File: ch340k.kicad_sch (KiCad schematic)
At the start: 8 parts, among them J1 USB_B_Mini, J2 Conn_01x06_Male, U1 CH340K

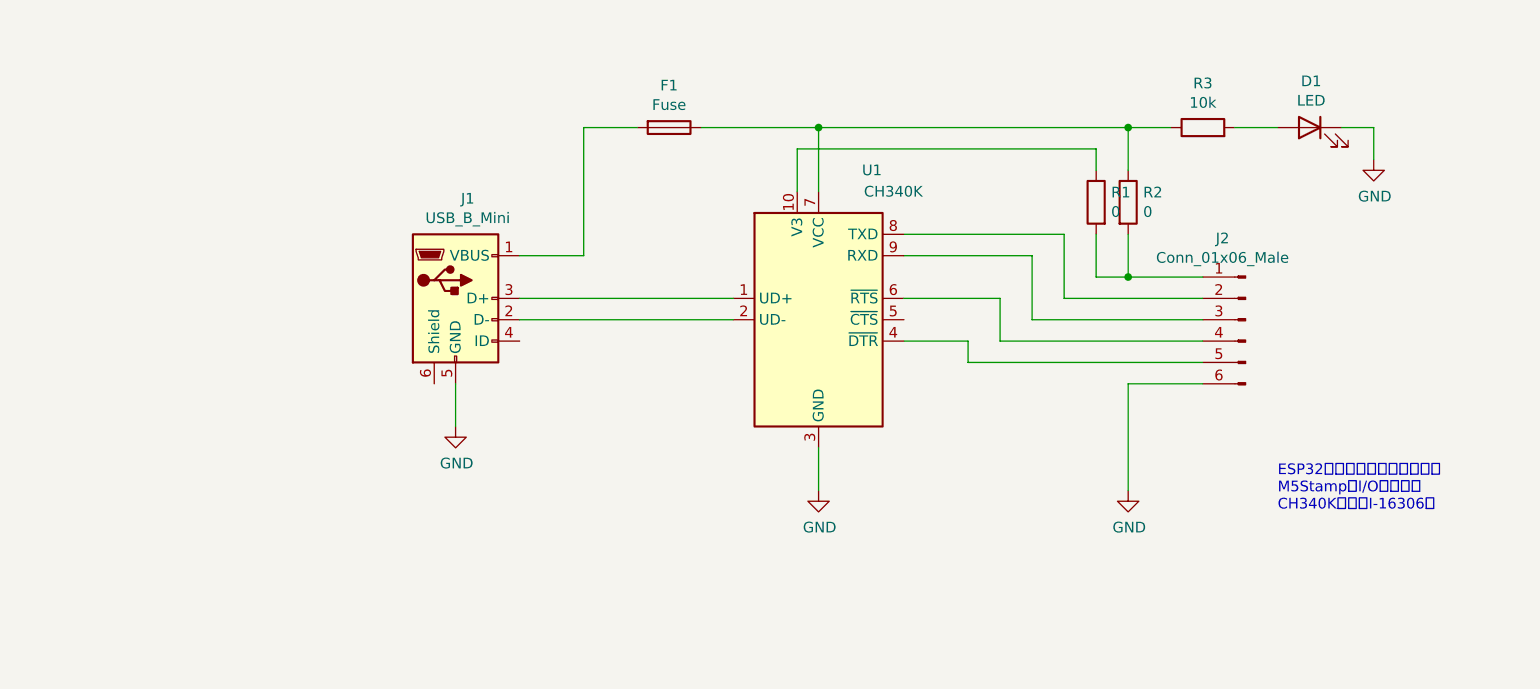
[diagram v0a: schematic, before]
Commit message: M5Stamp/ESP32 Downloader prototype
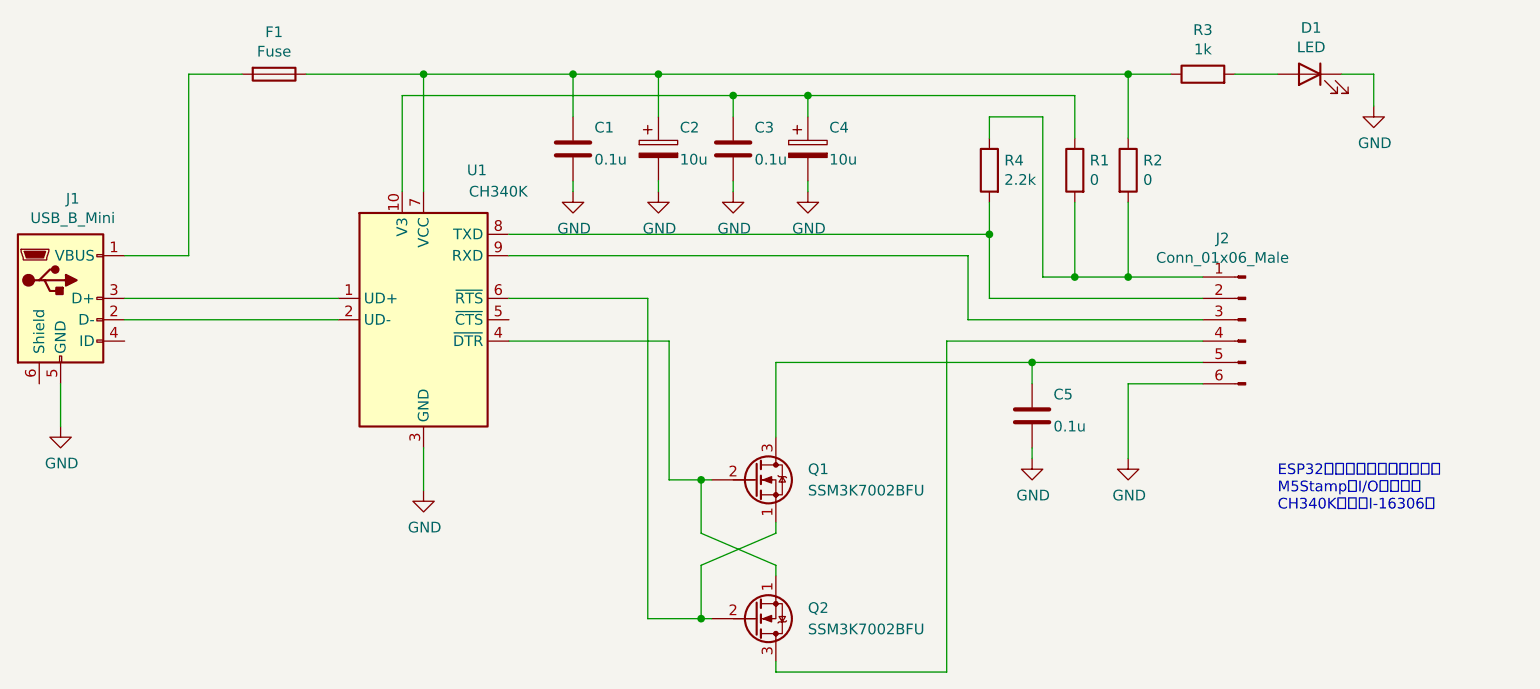
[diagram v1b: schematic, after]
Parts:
- added C1, C3, C5: 0.1u, UserLib:0603, symbol Device:C
- added C2, C4: 10u, Capacitor_THT:CP_Radial_D5.0mm_P2.00mm, symbol Device:C_Polarized
- added Q1, Q2: SSM3K7002BFU, Package_TO_SOT_SMD:SOT-323_SC-70, symbol Device:Q_NMOS_SGD
- added R4: 2.2k, UserLib:0603, symbol Device:R
- D1: footprint digikey-footprints:LED_2-SMD_No_Lead_1.7x0.8mm -> UserLib:0603
- F1, R1, R2: footprint digikey-footprints:0603 -> UserLib:0603
- R3: value 10k -> 1k; footprint digikey-footprints:0603 -> UserLib:0603
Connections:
- net GND: now also C1.2, C2.2, C3.2, C4.2, C5.2
- net at J2.1 (Pin_1), R1.2, R2.2: now also R4.1
- net at J2.2 (Pin_2), U1.8 (TXD): now also R4.2
- net at J2.4 (Pin_4): now also Q2.3 (D); no longer U1.6 (~{RTS})
- net at J2.5 (Pin_5): now also C5.1, Q1.3 (D); no longer U1.4 (~{DTR})
- net at R1.1, U1.10 (V3): now also C3.1, C4.1
- net at F1.1, R2.1, R3.1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: now also C1.1, C2.1
- new net: Q1.2 (G), Q2.1 (S), U1.4 (~{DTR})
- new net: Q1.1 (S), Q2.2 (G), U1.6 (~{RTS})
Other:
- moved on the sheet: D1, F1, J1, R1, R2, R3, U1

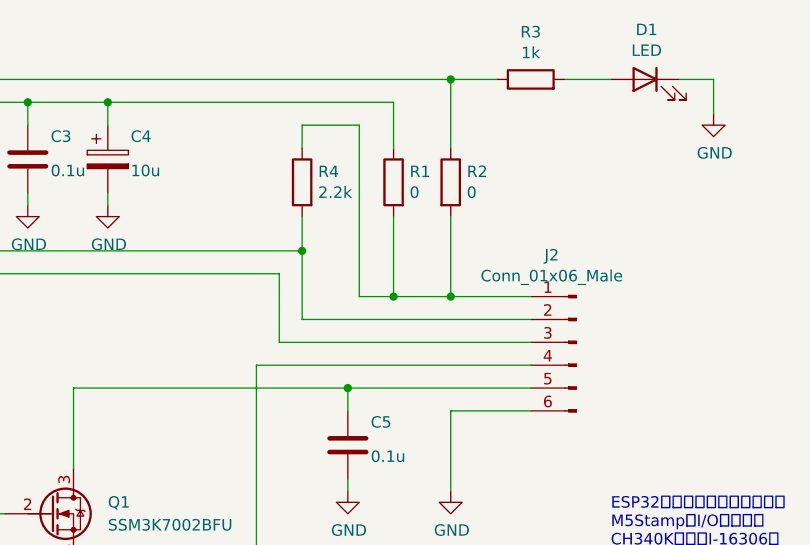
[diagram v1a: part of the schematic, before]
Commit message: Add files via upload
秋月の通販コード追加
部品表の代わりにxmlファイル
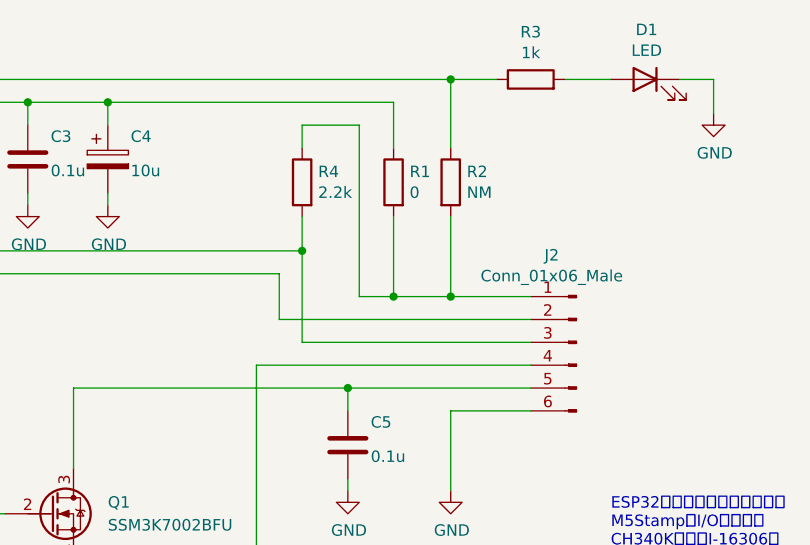
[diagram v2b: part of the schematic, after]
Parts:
- R2: value 0 -> NM
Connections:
- net at R4.2, U1.8 (TXD): now also J2.3 (Pin_3); no longer J2.2 (Pin_2)
- net at U1.9 (RXD): now also J2.2 (Pin_2); no longer J2.3 (Pin_3)
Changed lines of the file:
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@@
   (title_block
     (title "M5Stamp Downloader")
-    (date "2022-03-12")
+    (date "2022-05-03")
     (rev "0")
     (company "JK1MLY")
@@
     (stroke (width 0) (type default) (color 0 0 0 0))
   )
-  (wire (pts (xy 186.69 92.71) (xy 158.75 92.71))
+  (wire (pts (xy 186.69 92.71) (xy 161.29 92.71))
     (stroke (width 0) (type default) (color 0 0 0 0))
   )
@@
     (stroke (width 0) (type default) (color 0 0 0 0))
   )
-  (wire (pts (xy 186.69 90.17) (xy 161.29 90.17))
-    (stroke (width 0) (type default) (color 0 0 0 0))
-  )
   (wire (pts (xy 161.29 71.12) (xy 161.29 68.58))
     (stroke (width 0) (type default) (color 0 0 0 0))
@@
     (stroke (width 0) (type default) (color 0 0 0 0))
   )
+  (wire (pts (xy 186.69 90.17) (xy 158.75 90.17))
+    (stroke (width 0) (type default) (color 0 0 0 0))
+  )
   (wire (pts (xy 58.42 85.09) (xy 66.04 85.09))
     (stroke (width 0) (type default) (color 0 0 0 0))
@@
     (stroke (width 0) (type default) (color 0 0 0 0))
   )
-  (wire (pts (xy 158.75 92.71) (xy 158.75 85.09))
+  (wire (pts (xy 158.75 85.09) (xy 158.75 90.17))
     (stroke (width 0) (type default) (color 0 0 0 0))
   )
@@
     (stroke (width 0) (type default) (color 0 0 0 0))
   )
-  (wire (pts (xy 161.29 90.17) (xy 161.29 82.55))
+  (wire (pts (xy 161.29 82.55) (xy 161.29 92.71))
     (stroke (width 0) (type default) (color 0 0 0 0))
   )
@@
       (effects (font (size 1.27 1.27)) hide)
     )
-    (property "Datasheet" "~" (id 3) (at 191.77 92.71 0)
+    (property "Datasheet" "C-01627" (id 3) (at 191.77 92.71 0)
       (effects (font (size 1.27 1.27)) hide)
     )
@@
       (effects (font (size 1.27 1.27)) (justify left))
     )
-    (property "Value" "0" (id 1) (at 179.578 76.073 0)
+    (property "Value" "NM" (id 1) (at 179.578 76.073 0)
       (effects (font (size 1.27 1.27)) (justify left))
     )
@@
       (effects (font (size 1.27 1.27)) hide)
     )
-    (property "Datasheet" "" (id 3) (at 133.35 111.76 0)
+    (property "Datasheet" "I-08576" (id 3) (at 133.35 111.76 0)
       (effects (font (size 1.27 1.27)) hide)
     )
@@
       (effects (font (size 1.27 1.27)) hide)
     )
-    (property "Datasheet" "" (id 3) (at 111.76 72.39 0)
+    (property "Datasheet" "P-16143" (id 3) (at 111.76 72.39 0)
       (effects (font (size 1.27 1.27)) hide)
     )
@@
       (effects (font (size 1.27 1.27)) hide)
     )
-    (property "Datasheet" "~" (id 3) (at 139.7 72.39 0)
+    (property "Datasheet" "P-10590" (id 3) (at 139.7 72.39 0)
       (effects (font (size 1.27 1.27)) hide)
     )
@@
       (effects (font (size 1.27 1.27)) hide)
     )
-    (property "Datasheet" "" (id 3) (at 121.92 72.39 0)
+    (property "Datasheet" "P-10590" (id 3) (at 121.92 72.39 0)
       (effects (font (size 1.27 1.27)) hide)
     )
@@
       (effects (font (size 1.27 1.27)) hide)
     )
-    (property "Datasheet" "~" (id 3) (at 166.37 104.14 0)
+    (property "Datasheet" "P-16143" (id 3) (at 166.37 104.14 0)
       (effects (font (size 1.27 1.27)) hide)
     )
@@
       (effects (font (size 1.27 1.27)) hide)
     )
-    (property "Datasheet" "~" (id 3) (at 130.81 72.39 0)
+    (property "Datasheet" "P-16143" (id 3) (at 130.81 72.39 0)
       (effects (font (size 1.27 1.27)) hide)
     )
@@
     )
     (path "/00000000-0000-0000-0000-0000629f448e"
-      (reference "R2") (unit 1) (value "0") (footprint "UserLib:0603")
+      (reference "R2") (unit 1) (value "NM") (footprint "UserLib:0603")
     )
     (path "/00000000-0000-0000-0000-0000629fc2f1"
